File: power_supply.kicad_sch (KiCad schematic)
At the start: 32 parts, among them CON1 USB_B_Micro, CON2 Barrel_Jack_MountingPin, Q1 AO3401A, U1 AP1117-33, U2 AP6503, U3 CP2102N

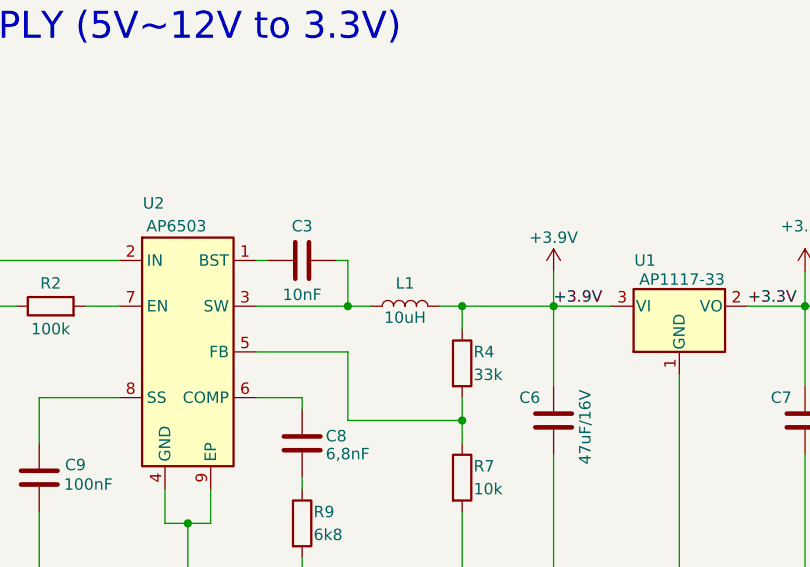
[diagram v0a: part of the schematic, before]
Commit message: Inserido ferrite bead para cada sheet
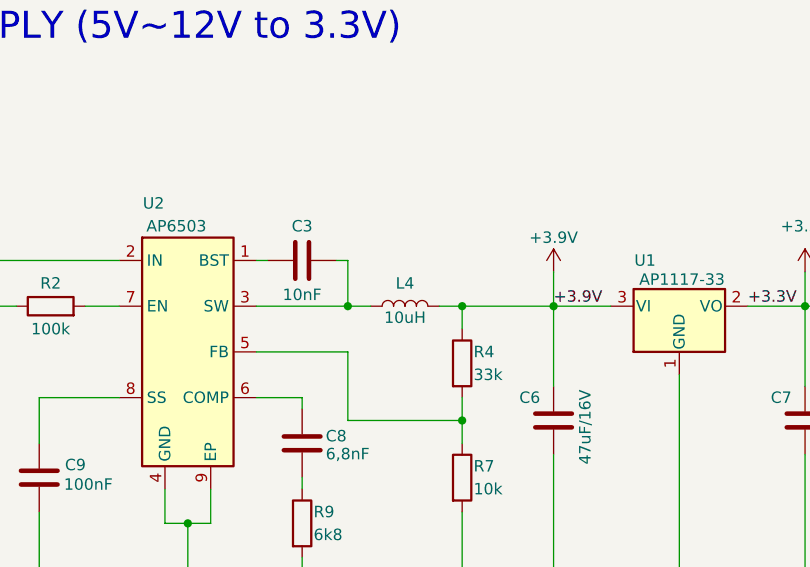
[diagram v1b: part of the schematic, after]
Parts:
- renumbered L1 to L4

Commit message: Continuando a adição dos hierarchical labels
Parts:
- R1, R5: value 1k -> (none)
- R10, R2: value 100k -> (none); footprint Resistor_SMD:R_0402_1005Metric_Pad0.72x0.64mm_HandSolder -> (none)
- R11: value 100k -> (none)
- R3: value 22k -> (none)
- R4: value 33k -> (none)
- R6: value 47k -> (none)
- R7, R8: value 10k -> (none)
- R9: value 6k8 -> (none)
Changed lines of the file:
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@@
       (effects (font (size 1.27 1.27)) (justify left))
     )
-    (property "Value" "1k" (id 1) (at 140.97 62.23 0)
+    (property "Value" "" (id 1) (at 140.97 62.23 0)
       (effects (font (size 1.27 1.27)) (justify left))
     )
@@
       (effects (font (size 1.27 1.27)) (justify left))
     )
-    (property "Value" "10k" (id 1) (at 93.98 73.66 0)
+    (property "Value" "" (id 1) (at 93.98 73.66 0)
       (effects (font (size 1.27 1.27)) (justify left))
     )
@@
       (effects (font (size 1.27 1.27)) (justify left))
     )
-    (property "Value" "1k" (id 1) (at 200.66 43.18 0)
+    (property "Value" "" (id 1) (at 200.66 43.18 0)
       (effects (font (size 1.27 1.27)) (justify left))
     )
@@
     (in_bom yes) (on_board yes)
     (property "Reference" "R2" (id 0) (at 46.99 50.8 90))
-    (property "Value" "100k" (id 1) (at 46.99 55.88 90))
-    (property "Footprint" "Resistor_SMD:R_0402_1005Metric_Pad0.72x0.64mm_HandSolder" (id 2) (at 46.99 55.118 90)
+    (property "Value" "" (id 1) (at 46.99 55.88 90))
+    (property "Footprint" "" (id 2) (at 46.99 55.118 90)
       (effects (font (size 1.27 1.27)) hide)
     )
@@
       (effects (font (size 1.27 1.27)) (justify left))
     )
-    (property "Value" "10k" (id 1) (at 239.3081 74.6319 90)
+    (property "Value" "" (id 1) (at 239.3081 74.6319 90)
       (effects (font (size 1.27 1.27)) (justify left))
     )
@@
       (effects (font (size 1.27 1.27)) (justify left))
     )
-    (property "Value" "33k" (id 1) (at 93.98 60.96 0)
+    (property "Value" "" (id 1) (at 93.98 60.96 0)
       (effects (font (size 1.27 1.27)) (justify left))
     )
@@
       (effects (font (size 1.27 1.27)) (justify left))
     )
-    (property "Value" "22k" (id 1) (at 191.77 55.88 0)
+    (property "Value" "" (id 1) (at 191.77 55.88 0)
       (effects (font (size 1.27 1.27)) (justify left))
     )
@@
       (effects (font (size 1.27 1.27)) (justify left))
     )
-    (property "Value" "100k" (id 1) (at 110.49 180.34 0)
+    (property "Value" "" (id 1) (at 110.49 180.34 0)
       (effects (font (size 1.27 1.27)) (justify left))
     )
@@
       (effects (font (size 1.27 1.27)) (justify left))
     )
-    (property "Value" "6k8" (id 1) (at 76.2 78.74 0)
+    (property "Value" "" (id 1) (at 76.2 78.74 0)
       (effects (font (size 1.27 1.27)) (justify left))
     )
@@
     (in_bom yes) (on_board yes)
     (property "Reference" "R10" (id 0) (at 115.57 170.18 90))
-    (property "Value" "100k" (id 1) (at 115.57 175.26 90))
-    (property "Footprint" "Resistor_SMD:R_0402_1005Metric_Pad0.72x0.64mm_HandSolder" (id 2) (at 115.57 174.498 90)
+    (property "Value" "" (id 1) (at 115.57 175.26 90))
+    (property "Footprint" "" (id 2) (at 115.57 174.498 90)
       (effects (font (size 1.27 1.27)) hide)
     )
@@
       (effects (font (size 1.27 1.27)) (justify left))
     )
-    (property "Value" "47k" (id 1) (at 191.77 66.04 0)
-      (effects (font (size 1.27 1.27)) (justify left))
-    )
+    (property "Value" "" (id 1) (at 191.77 66.04 0)
+      (effects (font (size 1.27 1.27)) (justify left))
+    )

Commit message: Adicionado footprint para AP6503 (U2)
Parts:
- U2: value AP6503 -> (none)
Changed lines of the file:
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@@
     (in_bom yes) (on_board yes)
     (property "Reference" "U2" (id 0) (at 58.42 41.91 0))
-    (property "Value" "AP6503" (id 1) (at 60.96 44.45 0))
+    (property "Value" "" (id 1) (at 60.96 44.45 0))
     (property "Footprint" "" (id 2) (at 78.74 72.39 0)
       (effects (font (size 1.27 1.27)) hide)

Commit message: Corrigido alguns ERC e adicionado circuito DTR e RI do BG95
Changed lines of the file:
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@@
     (stroke (width 0) (type default) (color 0 0 0 0))
   )
-  (wire (pts (xy 229.87 49.53) (xy 237.49 49.53))
+  (wire (pts (xy 229.87 49.53) (xy 241.3 49.53))
     (stroke (width 0) (type default) (color 0 0 0 0))
   )
@@
     (stroke (width 0) (type default) (color 0 0 0 0))
   )
+  (wire (pts (xy 102.87 69.85) (xy 102.87 82.55))
+    (stroke (width 0) (type default) (color 0 0 0 0))
+  )
+  (wire (pts (xy 204.47 59.69) (xy 190.5 59.69))
+    (stroke (width 0) (type default) (color 0 0 0 0))
+  )
+  (wire (pts (xy 214.63 156.21) (xy 214.63 157.48))
+    (stroke (width 0) (type default) (color 0 0 0 0))
+  )
+  (wire (pts (xy 80.01 48.26) (xy 80.01 53.34))
+    (stroke (width 0) (type default) (color 0 0 0 0))
+  )
+  (wire (pts (xy 229.87 72.39) (xy 233.68 72.39))
+    (stroke (width 0) (type default) (color 0 0 0 0))
+  )
+  (wire (pts (xy 132.08 171.45) (xy 132.08 175.26))
+    (stroke (width 0) (type default) (color 0 0 0 0))
+  )
+  (wire (pts (xy 229.87 46.99) (xy 241.3 46.99))
+    (stroke (width 0) (type default) (color 0 0 0 0))
+  )
+  (wire (pts (xy 24.13 59.69) (xy 24.13 63.5))
+    (stroke (width 0) (type default) (color 0 0 0 0))
+  )
+  (wire (pts (xy 199.39 45.72) (xy 199.39 46.99))
+    (stroke (width 0) (type default) (color 0 0 0 0))
+  )
+  (wire (pts (xy 214.63 156.21) (xy 215.9 156.21))
+    (stroke (width 0) (type default) (color 0 0 0 0))
+  )
+  (wire (pts (xy 213.36 154.94) (xy 213.36 156.21))
+    (stroke (width 0) (type default) (color 0 0 0 0))
+  )
+  (wire (pts (xy 266.7 29.21) (xy 266.7 31.75))
+    (stroke (width 0) (type default) (color 0 0 0 0))
+  )
+  (wire (pts (xy 80.01 53.34) (xy 82.55 53.34))
+    (stroke (width 0) (type default) (color 0 0 0 0))
+  )
+  (wire (pts (xy 271.78 31.75) (xy 271.78 33.02))
+    (stroke (width 0) (type default) (color 0 0 0 0))
+  )
+  (wire (pts (xy 53.34 166.37) (xy 55.88 166.37))
+    (stroke (width 0) (type default) (color 0 0 0 0))
+  )
+  (wire (pts (xy 124.46 53.34) (xy 130.81 53.34))
+    (stroke (width 0) (type default) (color 0 0 0 0))
+  )
+  (wire (pts (xy 214.63 39.37) (xy 214.63 41.91))
+    (stroke (width 0) (type default) (color 0 0 0 0))
+  )
+  (wire (pts (xy 190.5 48.26) (xy 190.5 50.8))
+    (stroke (width 0) (type default) (color 0 0 0 0))
+  )
   (wire (pts (xy 153.67 113.03) (xy 153.67 114.3))
     (stroke (width 0) (type default) (color 0 0 0 0))
   )
-  (wire (pts (xy 102.87 69.85) (xy 102.87 82.55))
-    (stroke (width 0) (type default) (color 0 0 0 0))
-  )
-  (wire (pts (xy 204.47 59.69) (xy 190.5 59.69))
-    (stroke (width 0) (type default) (color 0 0 0 0))
-  )
-  (wire (pts (xy 214.63 156.21) (xy 214.63 157.48))
-    (stroke (width 0) (type default) (color 0 0 0 0))
-  )
-  (wire (pts (xy 80.01 48.26) (xy 80.01 53.34))
-    (stroke (width 0) (type default) (color 0 0 0 0))
-  )
-  (wire (pts (xy 229.87 72.39) (xy 233.68 72.39))
-    (stroke (width 0) (type default) (color 0 0 0 0))
-  )
-  (wire (pts (xy 132.08 171.45) (xy 132.08 175.26))
-    (stroke (width 0) (type default) (color 0 0 0 0))
-  )
-  (wire (pts (xy 229.87 46.99) (xy 237.49 46.99))
-    (stroke (width 0) (type default) (color 0 0 0 0))
-  )
-  (wire (pts (xy 24.13 59.69) (xy 24.13 63.5))
-    (stroke (width 0) (type default) (color 0 0 0 0))
-  )
-  (wire (pts (xy 199.39 45.72) (xy 199.39 46.99))
-    (stroke (width 0) (type default) (color 0 0 0 0))
-  )
-  (wire (pts (xy 214.63 156.21) (xy 215.9 156.21))
-    (stroke (width 0) (type default) (color 0 0 0 0))
-  )
-  (wire (pts (xy 213.36 154.94) (xy 213.36 156.21))
-    (stroke (width 0) (type default) (color 0 0 0 0))
-  )
-  (wire (pts (xy 266.7 29.21) (xy 266.7 31.75))
-    (stroke (width 0) (type default) (color 0 0 0 0))
-  )
-  (wire (pts (xy 80.01 53.34) (xy 82.55 53.34))
-    (stroke (width 0) (type default) (color 0 0 0 0))
-  )
-  (wire (pts (xy 271.78 31.75) (xy 271.78 33.02))
-    (stroke (width 0) (type default) (color 0 0 0 0))
-  )
-  (wire (pts (xy 53.34 166.37) (xy 55.88 166.37))
-    (stroke (width 0) (type default) (color 0 0 0 0))
-  )
-  (wire (pts (xy 124.46 53.34) (xy 130.81 53.34))
-    (stroke (width 0) (type default) (color 0 0 0 0))
-  )
-  (wire (pts (xy 214.63 39.37) (xy 214.63 41.91))
-    (stroke (width 0) (type default) (color 0 0 0 0))
-  )
-  (wire (pts (xy 190.5 48.26) (xy 190.5 50.8))
-    (stroke (width 0) (type default) (color 0 0 0 0))
-  )
   (wire (pts (xy 261.62 31.75) (xy 266.7 31.75))
     (stroke (width 0) (type default) (color 0 0 0 0))
@@
     (stroke (width 0) (type default) (color 0 0 0 0))
   )
+  (polyline (pts (xy 160.02 121.92) (xy 284.48 121.92))
+    (stroke (width 0) (type default) (color 0 0 0 0))
+  )
+  (wire (pts (xy 190.5 58.42) (xy 190.5 59.69))
+    (stroke (width 0) (type default) (color 0 0 0 0))
+  )
+  (wire (pts (xy 80.01 66.04) (xy 92.71 66.04))
+    (stroke (width 0) (type default) (color 0 0 0 0))
+  )
+  (wire (pts (xy 102.87 53.34) (xy 102.87 62.23))
+    (stroke (width 0) (type default) (color 0 0 0 0))
+  )
+  (wire (pts (xy 116.84 82.55) (xy 116.84 60.96))
+    (stroke (width 0) (type default) (color 0 0 0 0))
+  )
+  (wire (pts (xy 266.7 31.75) (xy 271.78 31.75))
+    (stroke (width 0) (type default) (color 0 0 0 0))
+  )
+  (wire (pts (xy 59.69 161.29) (xy 53.34 161.29))
+    (stroke (width 0) (type default) (color 0 0 0 0))
+  )
   (wire (pts (xy 147.32 113.03) (xy 153.67 113.03))
     (stroke (width 0) (type default) (color 0 0 0 0))
   )
-  (polyline (pts (xy 160.02 121.92) (xy 284.48 121.92))
-    (stroke (width 0) (type default) (color 0 0 0 0))
-  )
-  (wire (pts (xy 190.5 58.42) (xy 190.5 59.69))
-    (stroke (width 0) (type default) (color 0 0 0 0))
-  )
-  (wire (pts (xy 80.01 66.04) (xy 92.71 66.04))
-    (stroke (width 0) (type default) (color 0 0 0 0))
-  )
-  (wire (pts (xy 102.87 53.34) (xy 102.87 62.23))
-    (stroke (width 0) (type default) (color 0 0 0 0))
-  )
-  (wire (pts (xy 116.84 82.55) (xy 116.84 60.96))
-    (stroke (width 0) (type default) (color 0 0 0 0))
-  )
-  (wire (pts (xy 266.7 31.75) (xy 271.78 31.75))
-    (stroke (width 0) (type default) (color 0 0 0 0))
-  )
-  (wire (pts (xy 59.69 161.29) (xy 53.34 161.29))
-    (stroke (width 0) (type default) (color 0 0 0 0))
-  )
   (wire (pts (xy 213.36 156.21) (xy 214.63 156.21))
     (stroke (width 0) (type default) (color 0 0 0 0))
@@
     (effects (font (size 2.9972 2.9972)) (justify left bottom))
   )
-  (label "GND" (at 153.67 113.03 180)
-    (effects (font (size 1.27 1.27)) (justify right bottom))
-  )
   (label "+5VD" (at 238.76 139.7 0)
     (effects (font (size 1.27 1.27)) (justify left bottom))
@@
     (effects (font (size 1.27 1.27)) (justify right bottom))
   )
-  (label "RXD" (at 237.49 49.53 180)
+  (label "UART0_RXD" (at 241.3 49.53 180)
     (effects (font (size 1.27 1.27)) (justify right bottom))
   )
@@
     (effects (font (size 1.27 1.27)) (justify right bottom))
   )
-  (label "TXD" (at 237.49 46.99 180)
+  (label "UART0_TXD" (at 241.3 46.99 180)
     (effects (font (size 1.27 1.27)) (justify right bottom))
   )
@@
     (effects (font (size 1.27 1.27)) (justify right))
   )
-  (hierarchical_label "UART0_TXD" (shape output) (at 237.49 46.99 0)
+  (hierarchical_label "UART0_TXD" (shape output) (at 241.3 46.99 0)
     (effects (font (size 1.27 1.27)) (justify left))
   )
@@
     (effects (font (size 1.27 1.27)) (justify right))
   )
-  (hierarchical_label "UART0_RXD" (shape input) (at 237.49 49.53 0)
+  (hierarchical_label "UART0_RXD" (shape input) (at 241.3 49.53 0)
     (effects (font (size 1.27 1.27)) (justify left))
   )

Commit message: Correções de ECR-Electrical Rules Checker
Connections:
- net GNDREF renamed GND

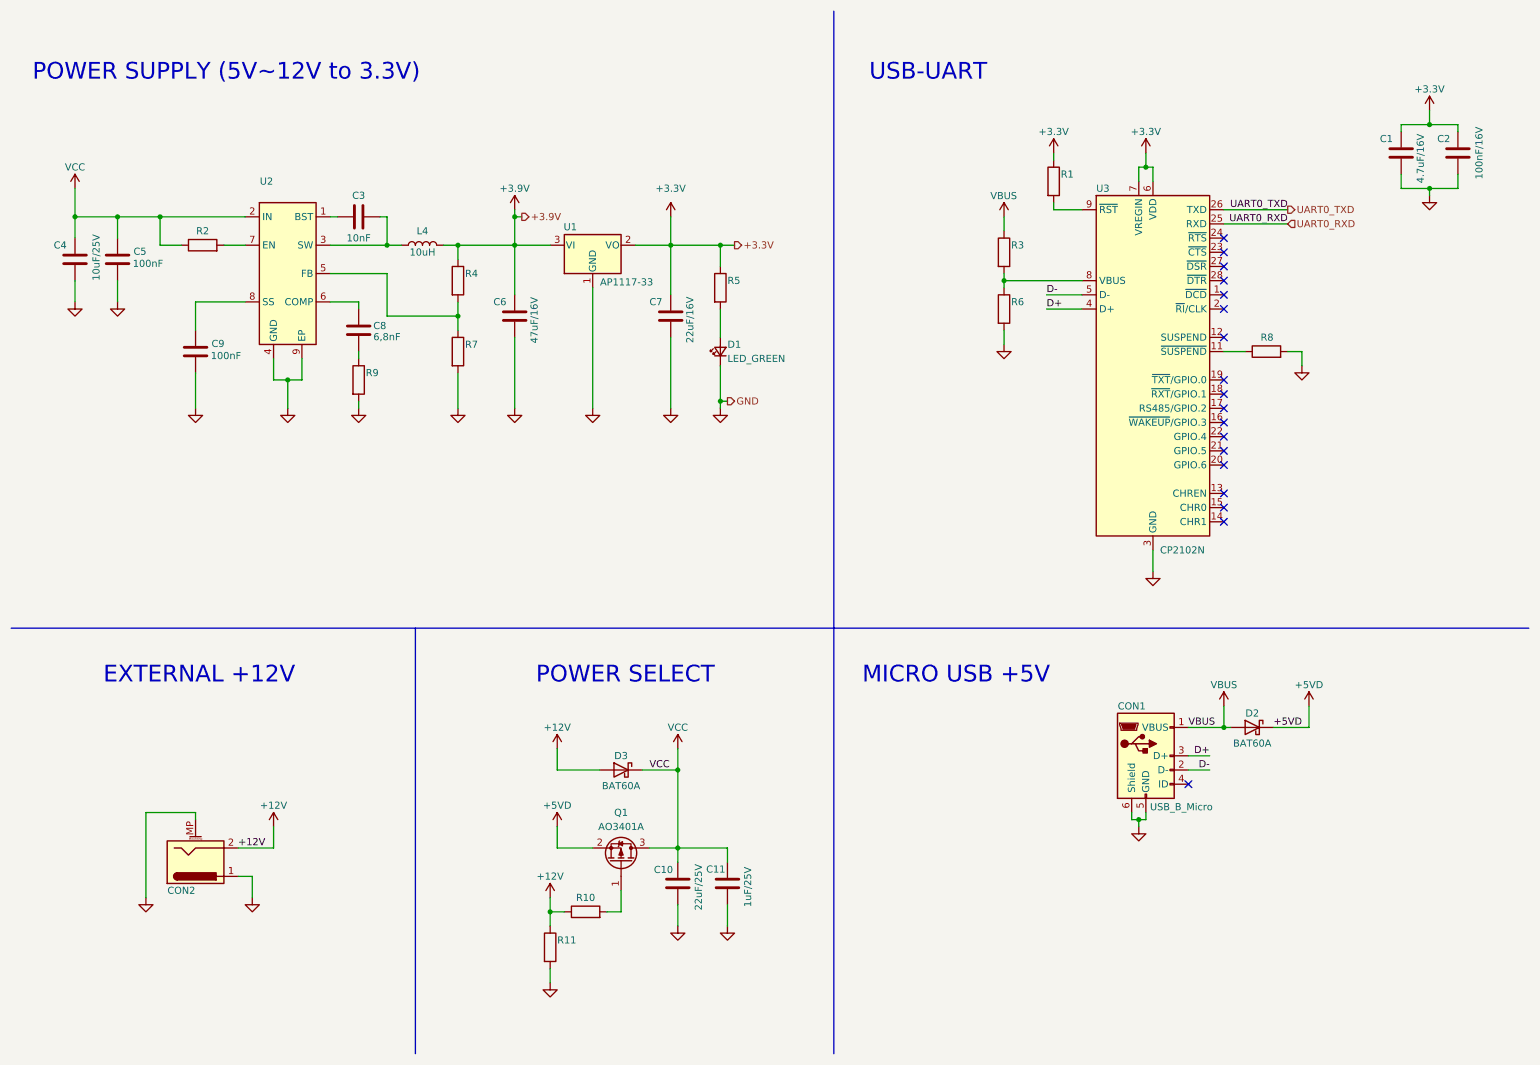
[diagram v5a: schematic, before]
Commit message: Corrigido todos os ERC
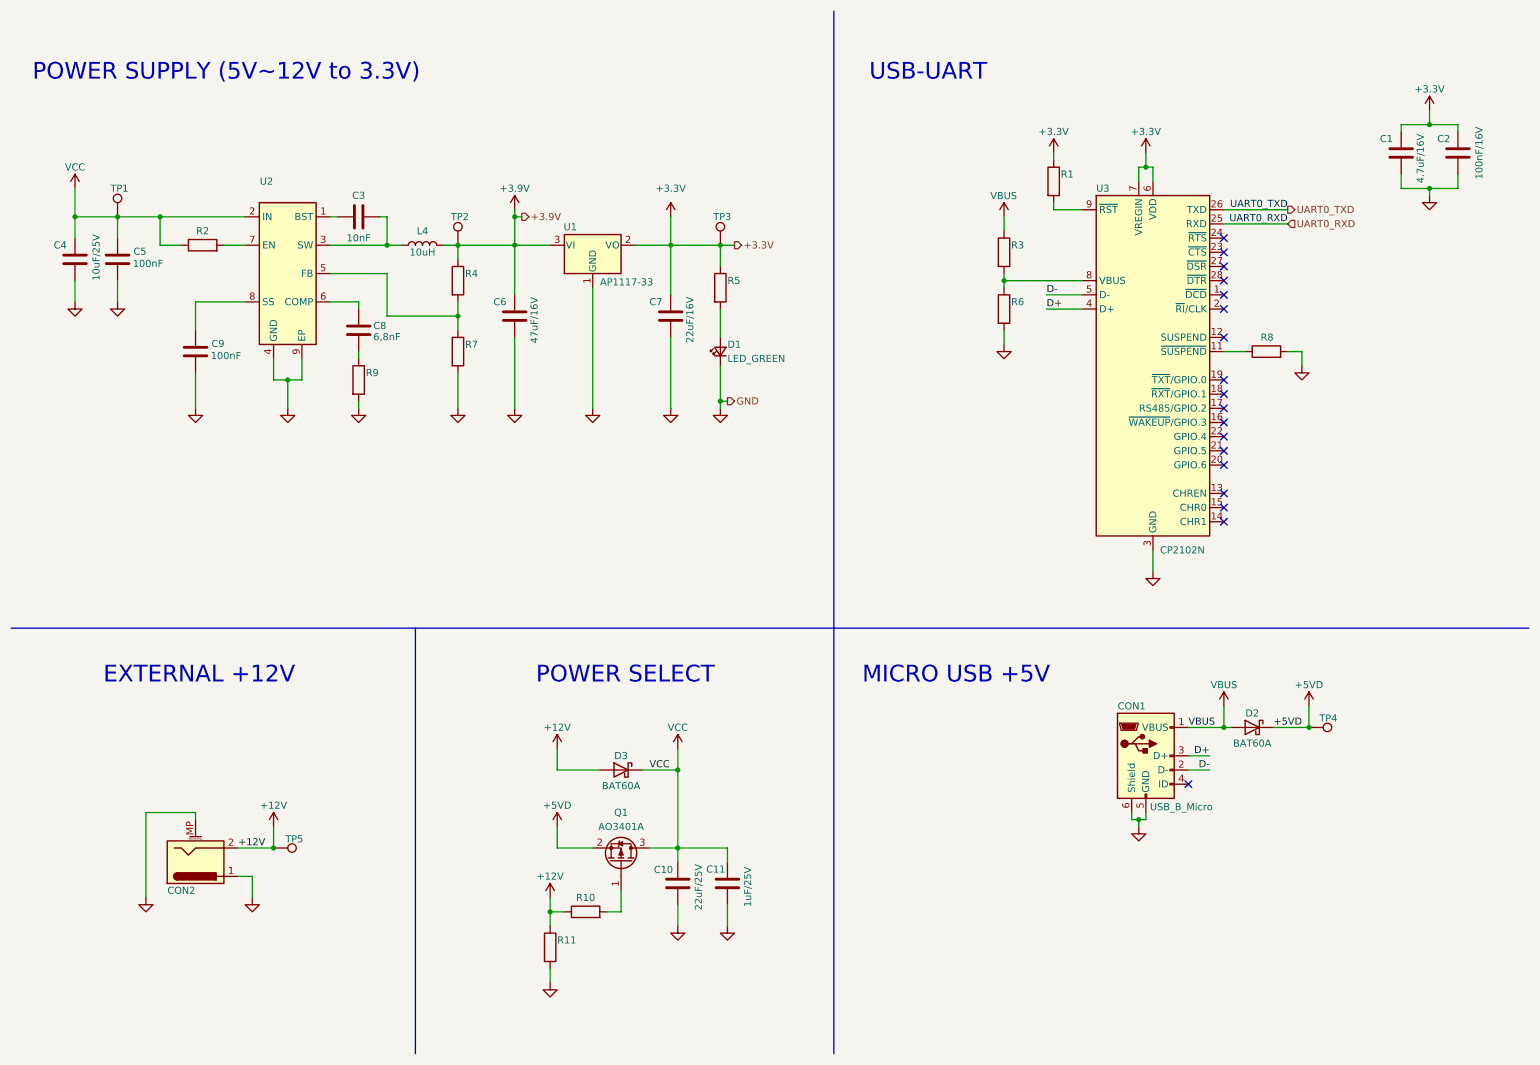
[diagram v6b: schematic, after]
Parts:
- added TP1: (no value), symbol Connector:TestPoint
- added TP2, TP3, TP4, TP5: TestPoint, symbol Connector:TestPoint
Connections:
- net +12V: now also TP5.1
- net +3.9V: now also TP2.1
- net +3V3: now also TP3.1
- net +5VD: now also TP4.1
- net VCC: now also TP1.1

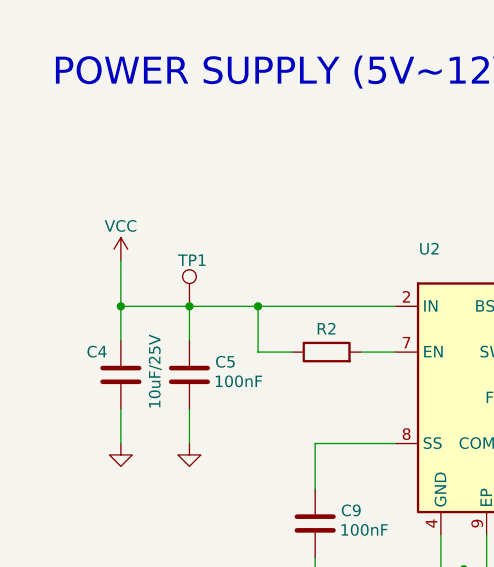
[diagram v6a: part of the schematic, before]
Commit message: Adicionado duas barras de pinos 1x10
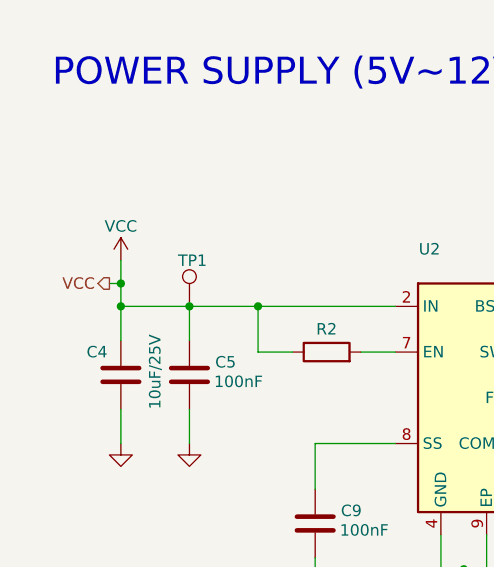
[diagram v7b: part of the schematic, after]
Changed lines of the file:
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@@
   (junction (at 132.08 161.29) (diameter 0) (color 0 0 0 0)
+  )
+  (junction (at 24.13 45.72) (diameter 0) (color 0 0 0 0)
   )
   (junction (at 245.11 139.7) (diameter 0) (color 0 0 0 0)
@@
     (stroke (width 0) (type default) (color 0 0 0 0))
   )
-  (wire (pts (xy 24.13 43.18) (xy 24.13 48.26))
+  (wire (pts (xy 24.13 43.18) (xy 24.13 45.72))
+    (stroke (width 0) (type default) (color 0 0 0 0))
+  )
+  (wire (pts (xy 22.86 45.72) (xy 24.13 45.72))
     (stroke (width 0) (type default) (color 0 0 0 0))
   )
@@
   )
   (wire (pts (xy 31.75 48.26) (xy 31.75 52.07))
+    (stroke (width 0) (type default) (color 0 0 0 0))
+  )
+  (wire (pts (xy 24.13 45.72) (xy 24.13 48.26))
     (stroke (width 0) (type default) (color 0 0 0 0))
   )
@@
     (effects (font (size 1.27 1.27)) (justify left))
   )
+  (hierarchical_label "VCC" (shape output) (at 22.86 45.72 180)
+    (effects (font (size 1.27 1.27)) (justify right))
+  )
   (hierarchical_label "UART0_RXD" (shape input) (at 241.3 49.53 0)
